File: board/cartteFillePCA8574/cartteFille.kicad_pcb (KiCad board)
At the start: 2 copper layers, 60 x 100 mm, 69 parts, among them U1 LM358, U201 PCA8574D,518, U202 PCA8574D,518, U21-2 SN74, U23-4 SN74, U25-6 SN74LVC2G14DBVTG4, U27-8 SN74LVC2G14DBVTG4

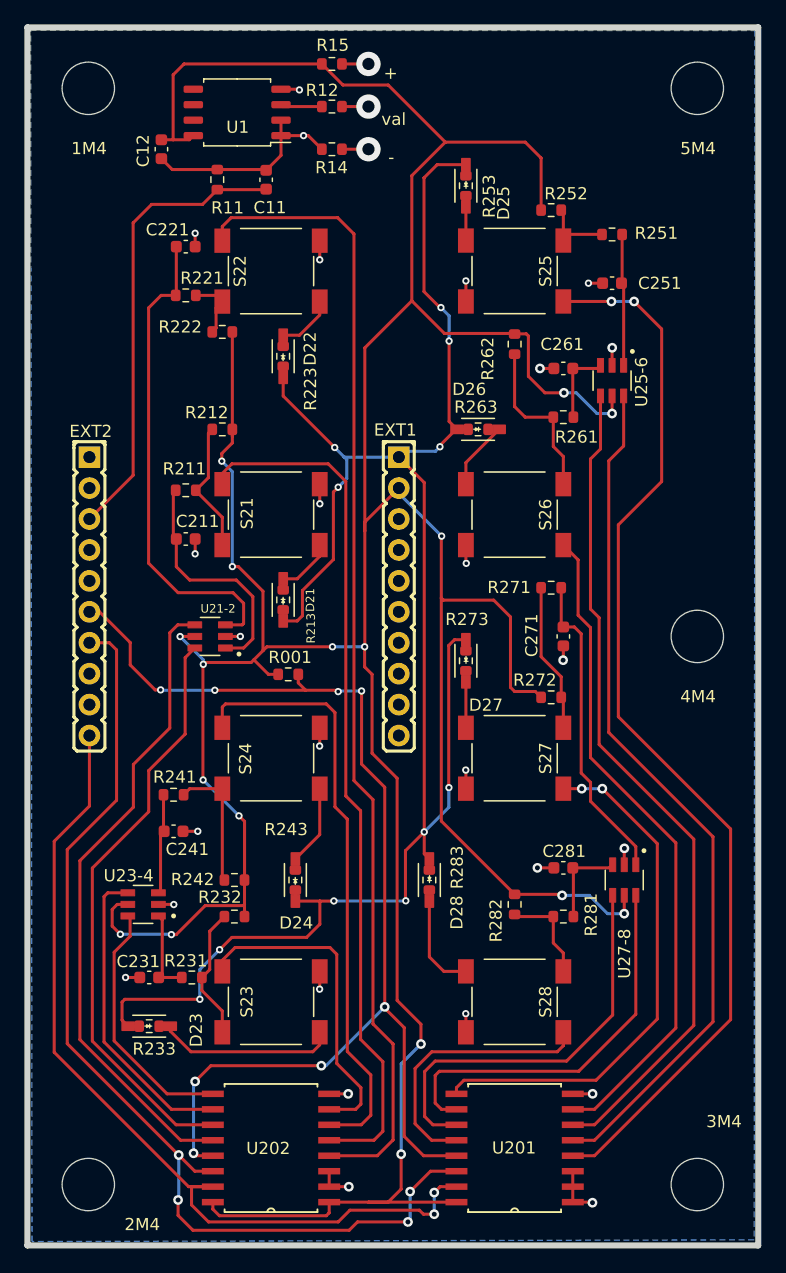
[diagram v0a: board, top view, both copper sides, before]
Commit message: commit_V2_PCB
seciond version of pcb final version with gerbert fils
ZIP of the gerber = gerbert_V2
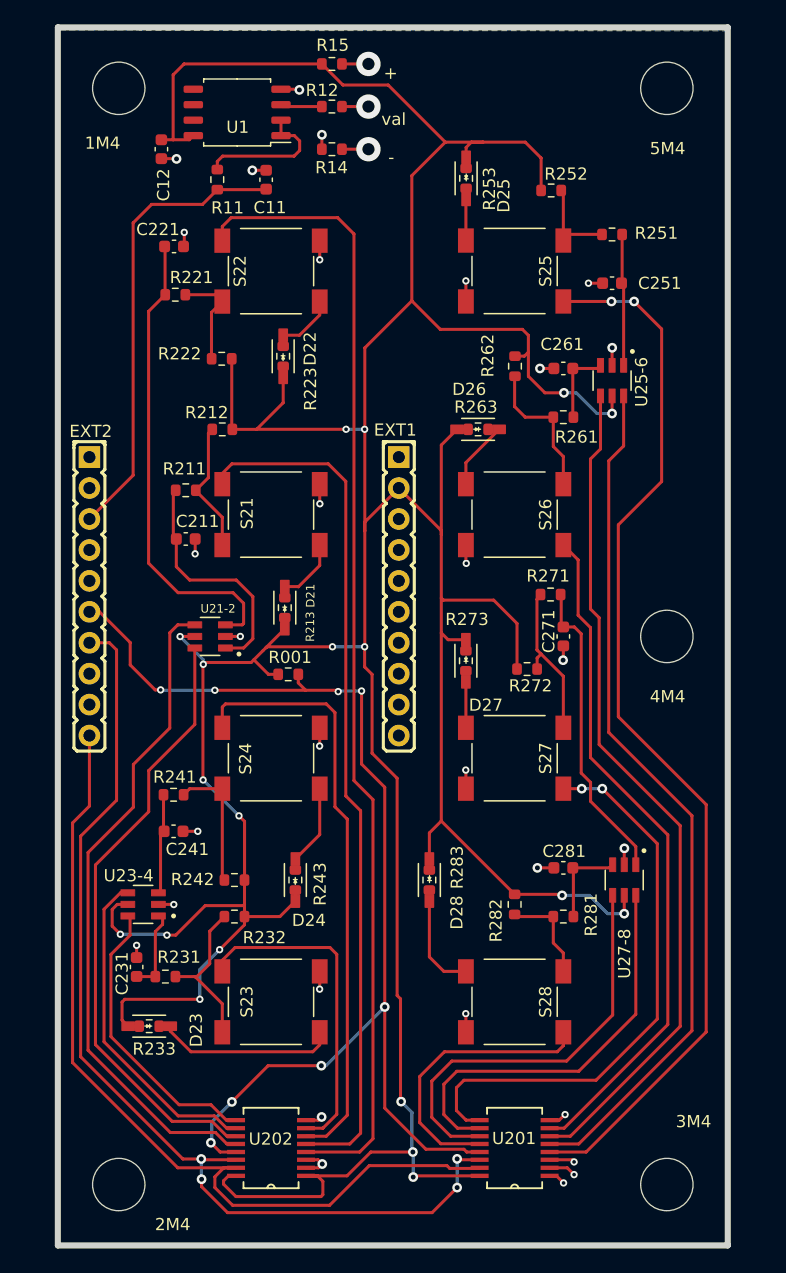
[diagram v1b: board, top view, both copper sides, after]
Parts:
- R11: value 10K -> 10KOhm
- R213, R223, R233, R243, R253, R263, R273, R283: value 150Ohm -> 68Ohm
- R232: value 1KOhm -> 1K
- R272: value 1K -> 1KOhm
- U201, U202: value PCA8574D,518 -> PCA8574PW,118; footprint PCA8574D_518:SOIC127P1032X265-16N -> SOP65P640X110-16N:SOP65P640X110-16N
- U21-2: value SN74 -> SN74LV
- moved R272 3.05 mm to (41.0, 52.7)
- moved 1M4 2.50 mm to (7.50, 5.00)
- moved 2M4 2.50 mm to (7.50, 95.0)
- moved 3M4 2.50 mm to (52.5, 95.0)
- moved 4M4 2.50 mm to (52.5, 50.0)
- moved 5M4 2.50 mm to (52.5, 5.00)
- moved R222 2.20 mm to (16.0, 27.2)
- moved R231 2.17 mm to (11.3, 77.9)
- moved R262 1.81 mm to (40.0, 27.8)
- moved R252 1.61 mm to (43.0, 13.4)
- moved C231 1.34 mm to (8.97, 77.1), turned to 90 degrees
- moved C221 0.96 mm to (12.0, 18.0)
- moved R221 0.86 mm to (12.1, 21.9)
- moved D21 0.65 mm to (21.1, 47.6)
- moved R213 0.65 mm to (21.1, 47.6)
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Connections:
- net /ADC_CH0-U11RP1 renamed /ADC_CH7-U11RP1
- D21 pad 2: +5V -> +3V3
- D22 pad 2: +5V -> +3V3
- D23 pad 2: +5V -> +3V3
- D24 pad 2: +5V -> +3V3
- D25 pad 2: +5V -> +3V3
- D26 pad 2: +5V -> +3V3
- D27 pad 2: +5V -> +3V3
- D28 pad 2: +5V -> +3V3
- R11 pad 1: GND -> Net-(R11-Pad1)
- R213 pad 2: +5V -> +3V3
- R223 pad 2: +5V -> +3V3
- R233 pad 2: +5V -> +3V3
- R243 pad 2: +5V -> +3V3
- R253 pad 2: +5V -> +3V3
- R263 pad 2: +5V -> +3V3
- R273 pad 2: +5V -> +3V3
- R283 pad 2: +5V -> +3V3
- U1 pad 1: GND -> Net-(R11-Pad1)
- U1 pad 2: GND -> Net-(R11-Pad1)
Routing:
- net +5V: track 157.9 -> 0.00 mm, vias 11 -> 0
- net +3V3: track 345.6 -> 381.8 mm, vias 17 -> 19
- net GND: track 56.3 -> 43.7 mm, vias 26 -> 30
- net Net-(R11-Pad1): track 0.00 -> 11.6 mm
- net /U201P4-S27LED: track 43.3 -> 46.9 mm
- net Net-(R221-Pad2): track 5.22 -> 8.33 mm
- net /U202P4-U234S23: track 20.8 -> 23.7 mm
- net /I2C_SCL: track 84.9 -> 82.6 mm
- net /GPIO32-INTB: track 96.4 -> 94.3 mm
- net Net-(R231-Pad2): track 11.0 -> 13.1 mm
- net /U202P6-U212S21: track 48.5 -> 50.6 mm
- net /U202P5-U234S24: track 25.2 -> 27.2 mm
- net Net-(R261-Pad2): track 13.7 -> 11.9 mm
- net /I2C_SDA: track 72.9 -> 71.2 mm, vias 2 -> 0
- net Net-(R251-Pad2): track 5.96 -> 7.58 mm
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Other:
- board size 60 x 100 mm -> 55 x 100 mm
